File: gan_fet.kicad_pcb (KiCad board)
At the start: 2 copper layers, 10.2 x 22.2 mm, 7 parts, among them J1 Conn_01x04_Male, Q1 EPC2036, U1 NPC81074

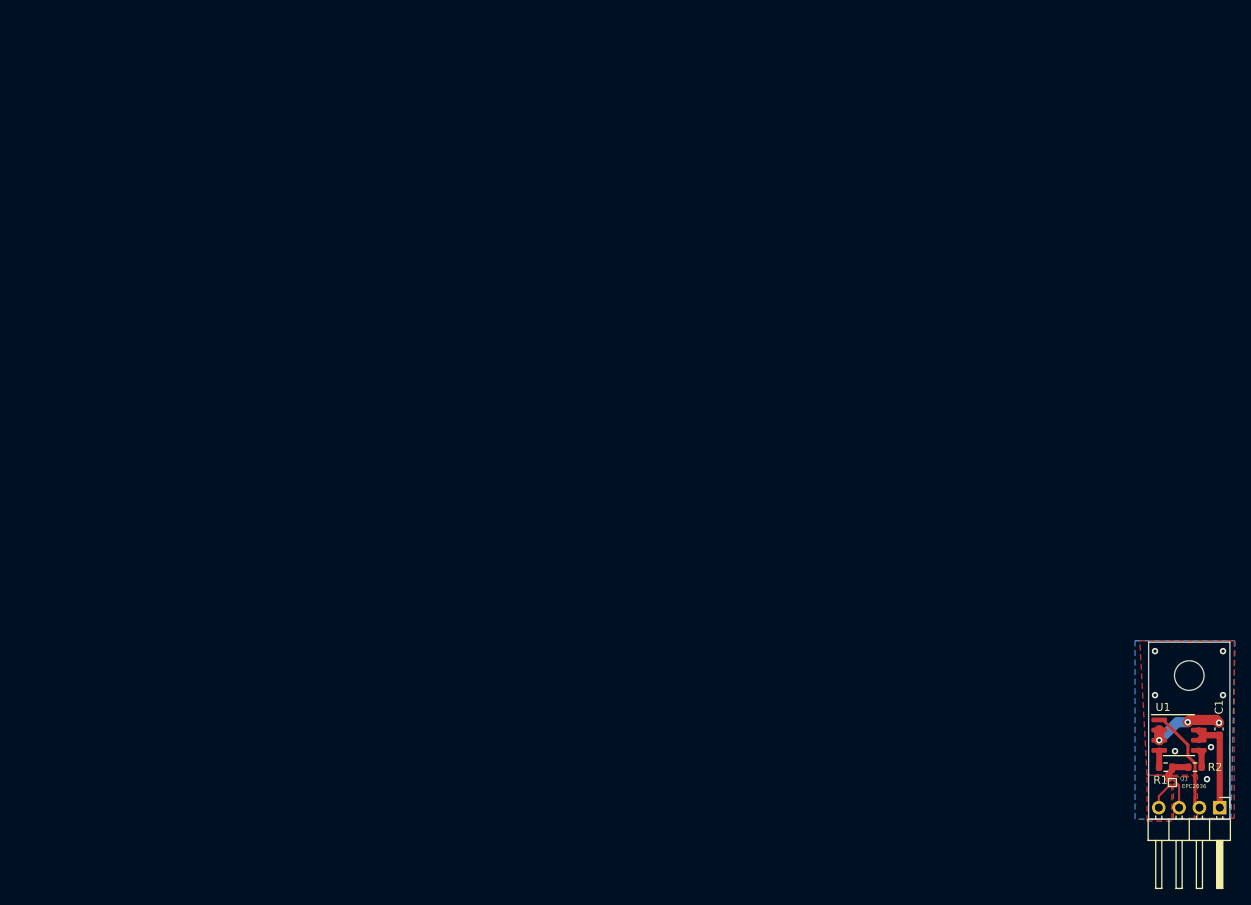
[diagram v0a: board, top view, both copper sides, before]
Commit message: Imported the traces using fcad_pcb macro instead of kSU
Moved PCB schematic to the origin to make part placement easier
Applied fixed temperatures for simulation rather than fixed power
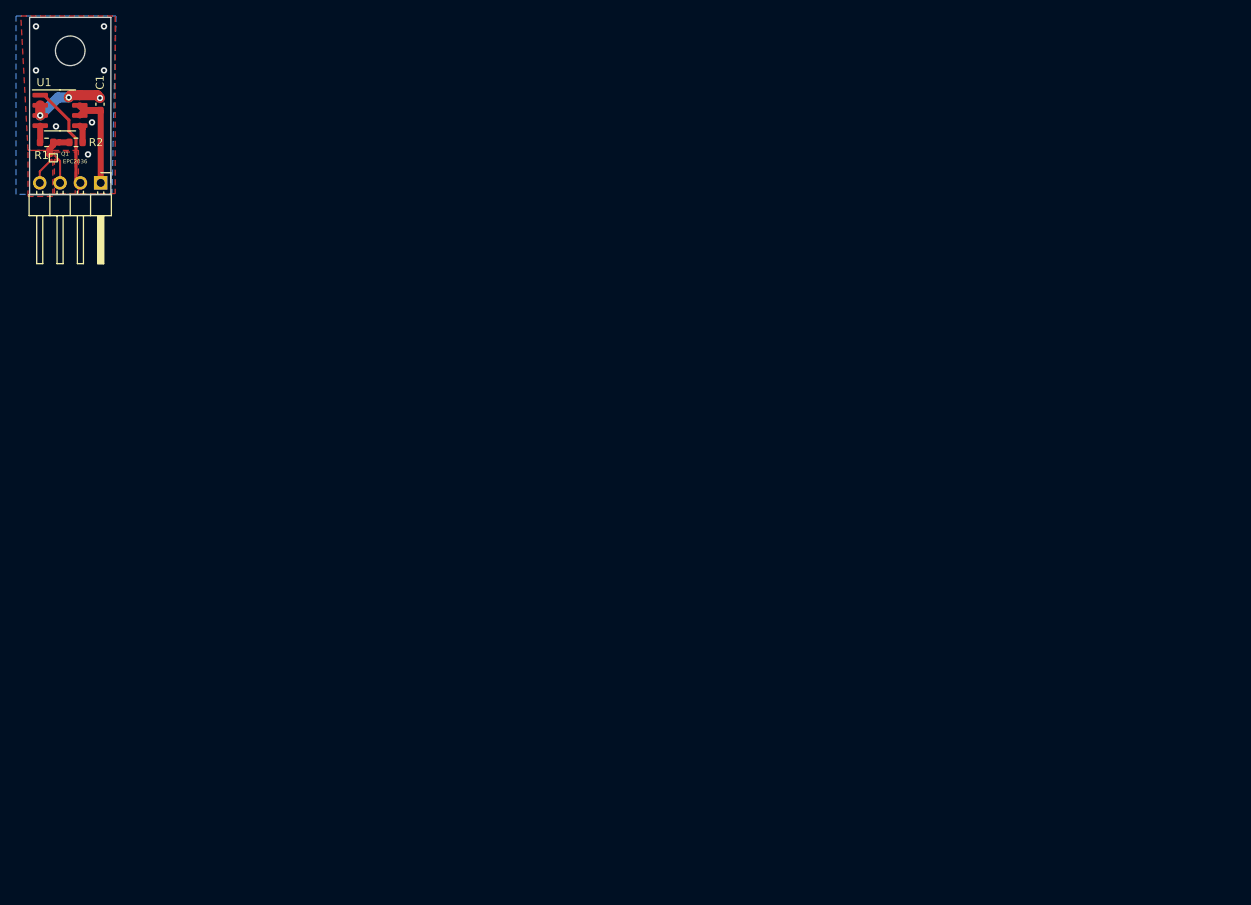
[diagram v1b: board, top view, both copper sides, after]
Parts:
- moved C1 160.2 mm to (8.62, 11.1)
- moved J1 160.2 mm to (8.71, 21.0)
- moved Q1 160.2 mm to (2.34, 18.3)
- moved R1 160.2 mm to (1.95, 15.9)
- moved R2 160.2 mm to (5.62, 15.9)
- moved REF** 160.2 mm to (4.90, 4.46)
- moved U1 160.2 mm to (3.62, 11.9)
